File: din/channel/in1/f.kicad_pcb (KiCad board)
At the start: 2 copper layers, 19.7 x 8.9 mm, 5 parts, among them J1 dio_channel_i, U1 LTV-357T

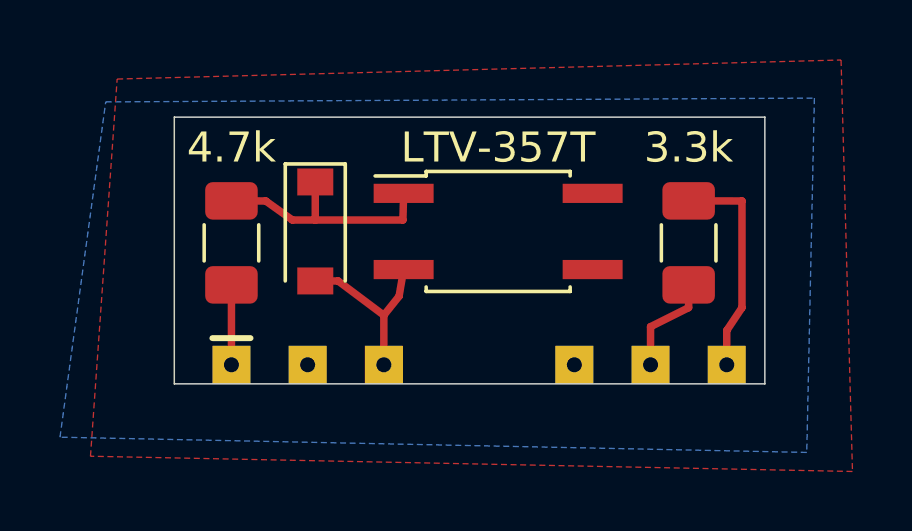
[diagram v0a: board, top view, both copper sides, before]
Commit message: voltage regulator for each module
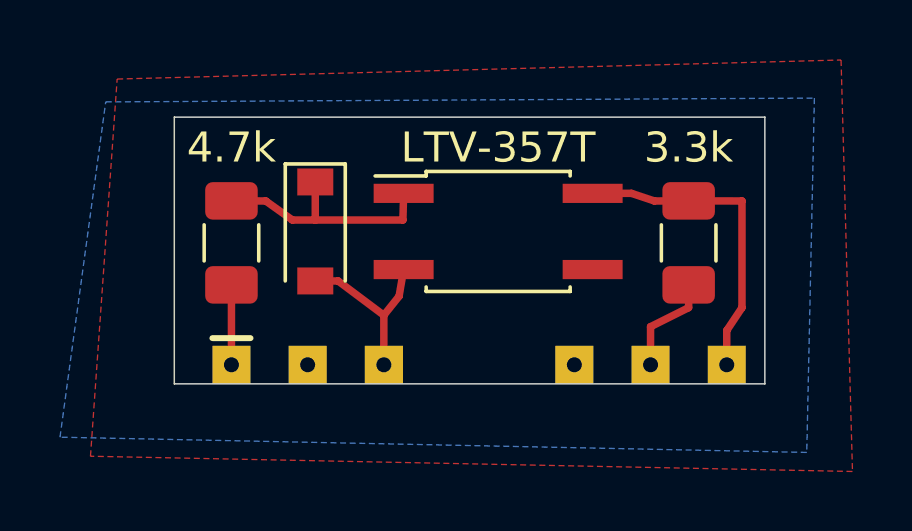
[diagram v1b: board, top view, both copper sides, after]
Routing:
- net OUT: track 7.39 -> 10.6 mm
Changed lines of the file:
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@@
     (thickness 0.8)
     (drawings 12)
-    (tracks 19)
+    (tracks 22)
     (zones 0)
     (modules 5)
@@
     (user_trace_width 0.3)
     (trace_clearance 0.2)
-    (zone_clearance 0.254)
+    (zone_clearance 0)
     (zone_45_only no)
     (trace_min 0.2)
@@
   (segment (start 145.288 109.22) (end 145.288 105.664) (width 0.25) (layer F.Cu) (net 1))
   (segment (start 145.288 105.664) (end 143.51 105.661) (width 0.25) (layer F.Cu) (net 1))
+  (segment (start 140.31 105.41) (end 141.605 105.41) (width 0.25) (layer F.Cu) (net 1))
+  (segment (start 141.605 105.41) (end 142.367 105.664) (width 0.25) (layer F.Cu) (net 1))
+  (segment (start 142.367 105.664) (end 143.51 105.661) (width 0.25) (layer F.Cu) (net 1))
   (segment (start 142.24 111.125) (end 142.24 109.855) (width 0.25) (layer F.Cu) (net 2))
   (segment (start 142.24 109.855) (end 143.51 109.22) (width 0.25) (layer F.Cu) (net 2))
@@
   (segment (start 131.064 106.299) (end 133.985 106.299) (width 0.25) (layer F.Cu) (net 7))
   (zone (net 3) (net_name GND) (layer F.Cu) (hatch edge 0.508)
-    (connect_pads (clearance 0.254))
-    (min_thickness 0.254)
-    (fill yes (arc_segments 32) (thermal_gap 0.3) (thermal_bridge_width 0.3))
+    (connect_pads (clearance 0))
+    (min_thickness 0.1)
+    (fill yes (arc_segments 32) (thermal_gap 0.3) (thermal_bridge_width 0.2))
     (polygon
       (pts
@@
   )
   (zone (net 3) (net_name GND) (layer B.Cu) (hatch edge 0.508)
-    (connect_pads (clearance 0.254))
-    (min_thickness 0.254)
-    (fill yes (arc_segments 32) (thermal_gap 0.3) (thermal_bridge_width 0.3))
+    (connect_pads (clearance 0))
+    (min_thickness 0.1)
+    (fill yes (arc_segments 32) (thermal_gap 0.3) (thermal_bridge_width 0.2))
     (polygon
       (pts
